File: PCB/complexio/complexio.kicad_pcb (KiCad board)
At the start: 2 copper layers, 69.1 x 144.1 mm, 107 parts, among them J1 Conn_01x21_Pin, J2 Conn_01x21_Pin, J3 USB_C_Receptacle_USB2.0_16P, J5 Conn_01x03_Pin, Q1 AO3400A, SW1 SW_SPDT, U1 MPU6050, U10 KTIR0711S, U11 KTIR0711S, U12 KTIR0711S, U13 KTIR0711S, U14 KTIR0711S, U15 KTIR0711S, U16 KTIR0711S, U17 KTIR0711S, U18 KTIR0711S, U19 KTIR0711S, U2 TB6612FNG, U20 SN74LVC16T245DGGR, U21 AT24CM01, U22 STM32F303RBT6, U23 AP2112K-3.3, U3 TB6612FNG, U4 KTIR0711S, U5 KTIR0711S, U6 KTIR0711S, U7 KTIR0711S, U8 KTIR0711S, U9 KTIR0711S

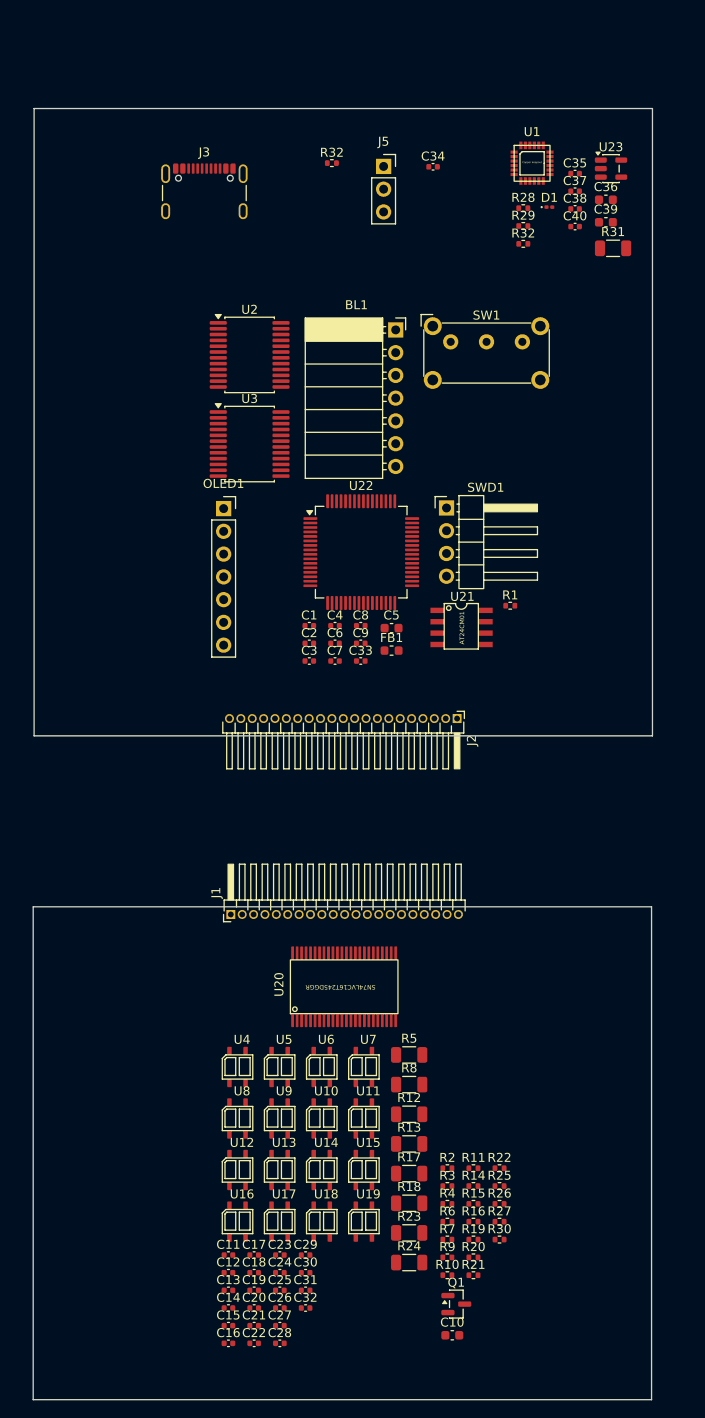
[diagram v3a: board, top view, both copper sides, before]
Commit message: Advanced with schem & resolved main power problem
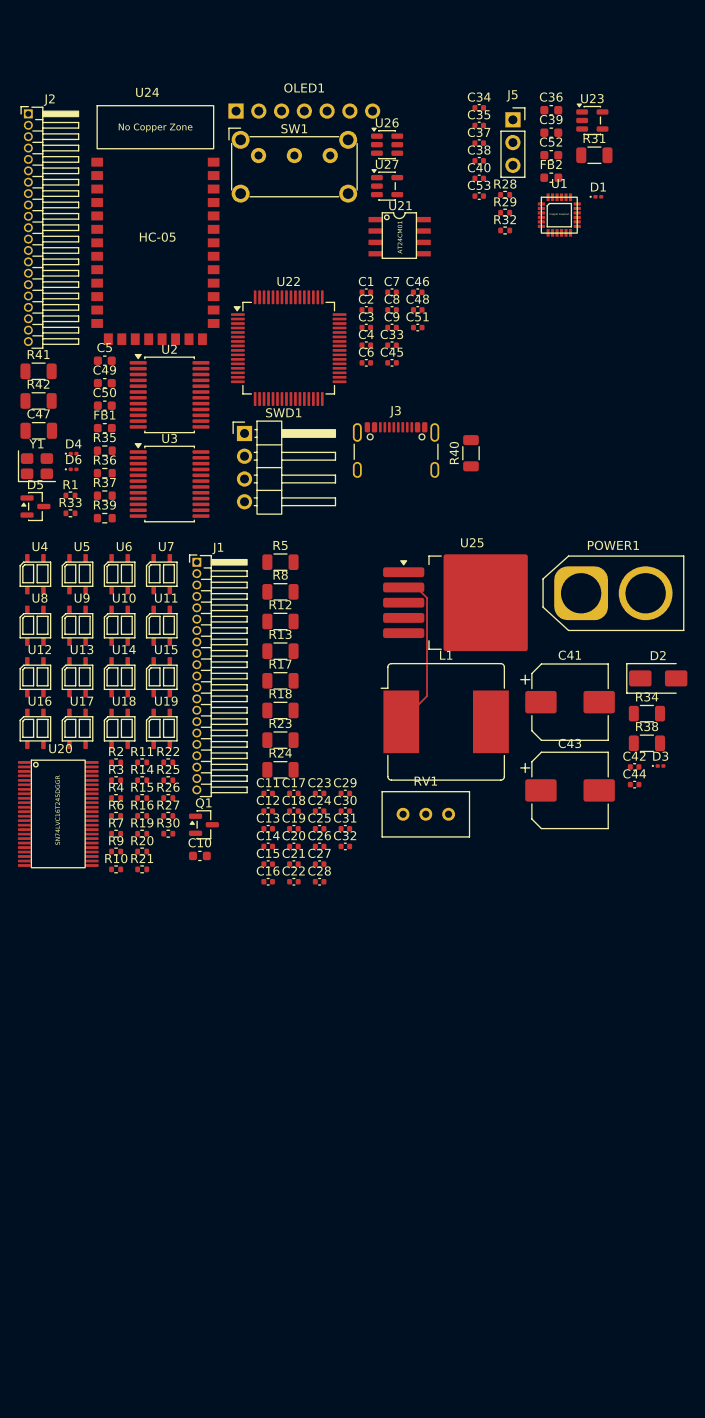
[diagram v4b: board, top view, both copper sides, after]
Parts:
- removed BL1: Bluetooth HC-05 module, Connector_PinSocket_2.54mm:PinSocket_1x07_P2.54mm_Horizontal
- removed the R32 at (116.2, 59.1)
- removed the R32 at (137.6, 68.1)
- added C41: 100u, Capacitor_SMD:CP_Elec_8x10, F.Cu at (142.8, 119.2)
- added C42: 100n, Capacitor_SMD:C_0402_1005Metric, F.Cu at (150.0, 126.5)
- added C43: 220u, Capacitor_SMD:CP_Elec_8x10, F.Cu at (142.8, 129.1)
- added C44: 100n, Capacitor_SMD:C_0402_1005Metric, F.Cu at (150.0, 128.4)
- added C45: 18p, Capacitor_SMD:C_0402_1005Metric, F.Cu at (122.9, 81.4)
- added C46: 18p, Capacitor_SMD:C_0402_1005Metric, F.Cu at (125.8, 73.5)
- added C47: 4n7, Capacitor_SMD:C_1206_3216Metric, F.Cu at (83.5, 89.0)
- added C48: 100n, Capacitor_SMD:C_0402_1005Metric, F.Cu at (125.8, 75.5)
- added C49: 4u7, Capacitor_SMD:C_0603_1608Metric, F.Cu at (90.9, 83.7)
- added C50: 10u, Capacitor_SMD:C_0603_1608Metric, F.Cu at (90.9, 86.2)
- added C51: 100n, Capacitor_SMD:C_0402_1005Metric, F.Cu at (125.8, 77.4)
- added C52: 10u, Capacitor_SMD:C_0603_1608Metric, F.Cu at (140.7, 58.2)
- added C53: 100n, Capacitor_SMD:C_0402_1005Metric, F.Cu at (132.7, 62.8)
- added D2: SS34, Diode_SMD:D_SMA, F.Cu at (152.6, 116.6)
- added D3: LED, LED_SMD:LED_0201_0603Metric, F.Cu at (152.9, 126.4)
- added D4: LED, LED_SMD:LED_0201_0603Metric, F.Cu at (87.4, 91.5)
- added D5: BAT54C, Package_TO_SOT_SMD:SOT-23, F.Cu at (83.2, 97.4)
- added D6: LED, LED_SMD:LED_0201_0603Metric, F.Cu at (87.4, 93.3)
- added FB2: 600R, Inductor_SMD:L_0603_1608Metric, F.Cu at (140.7, 60.7)
- added L1: 47uH, Inductor_SMD:L_Bourns_SRR1208_12.7x12.7mm, F.Cu at (129.0, 121.4)
- added POWER1: Conn_01x02_Socket, Connector_AMASS:AMASS_XT60-M_1x02_P7.20mm_Vertical, F.Cu at (144.0, 107.1)
- added R32: 4k7, Resistor_SMD:R_0402_1005Metric, F.Cu at (135.6, 66.6)
- added R33: 10k, Resistor_SMD:R_0402_1005Metric, F.Cu at (87.1, 98.2)
- added R34: 1k, Resistor_SMD:R_1206_3216Metric, F.Cu at (151.4, 120.5)
- added R35: 2k2, Resistor_SMD:R_0603_1608Metric, F.Cu at (90.9, 91.2)
- added R36: 2k2, Resistor_SMD:R_0603_1608Metric, F.Cu at (90.9, 93.7)
- added R37: 5k1, Resistor_SMD:R_0603_1608Metric, F.Cu at (90.9, 96.2)
- added R38: 1k, Resistor_SMD:R_1206_3216Metric, F.Cu at (151.4, 123.8)
- added R39: 5k1, Resistor_SMD:R_0603_1608Metric, F.Cu at (90.9, 98.7)
- added R40: 1M, Resistor_SMD:R_1206_3216Metric, F.Cu at (131.8, 91.5)
- added R41: 1k, Resistor_SMD:R_1206_3216Metric, F.Cu at (83.5, 82.3)
- added R42: 1k, Resistor_SMD:R_1206_3216Metric, F.Cu at (83.5, 85.6)
- added RV1: R_Potentiometer, Potentiometer_THT:Potentiometer_Bourns_3296W_Vertical, F.Cu at (129.2, 131.8)
- added U24: HC-05, HC-05:HC-05_SMD, F.Cu at (90.0, 52.7)
- added U25: LM2596S-ADJ, Package_TO_SOT_SMD:TO-263-5_TabPin3, F.Cu at (131.9, 108.1)
- added U26: USBLC6-2SC6, Package_TO_SOT_SMD:SOT-23-6, F.Cu at (122.4, 57.0)
- added U27: AP2112K-3.3, Package_TO_SOT_SMD:SOT-23-5, F.Cu at (122.4, 61.7)
- added Y1: 8MHz, Crystal:Crystal_SMD_3225-4Pin_3.2x2.5mm, F.Cu at (83.3, 92.9)
- OLED1: footprint Connector_PinSocket_2.54mm:PinSocket_1x07_P2.54mm_Vertical -> SSD1306_SPI:SSD1306_SPI
- moved J2 82.7 mm to (82.4, 53.6), turned to 0 degrees
- moved Q1 60.4 mm to (102.0, 132.9)
- moved C10 60.4 mm to (101.5, 136.4)
- moved U10 59.4 mm to (90.8, 108.5)
- moved U11 59.4 mm to (95.5, 108.5)
- moved U12 59.4 mm to (81.4, 114.2)
- moved U13 59.4 mm to (86.1, 114.2)
- moved U14 59.4 mm to (90.8, 114.2)
- moved U15 59.4 mm to (95.5, 114.2)
- moved U16 59.4 mm to (81.4, 120.0)
- moved U17 59.4 mm to (86.1, 120.0)
- moved U18 59.4 mm to (90.8, 120.0)
- moved U19 59.4 mm to (95.5, 120.0)
- moved U4 59.4 mm to (81.4, 102.7)
- moved U5 59.4 mm to (86.1, 102.7)
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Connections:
- net /PA14 renamed /SWCLK
- net Net-(J3-VBUS-PadA4) renamed VBUS_5V
- C10 pad 1: +5V -> BAT_5V
- C11 pad 1: +5V -> BAT_5V
- C12 pad 1: +5V -> BAT_5V
- C13 pad 1: +5V -> BAT_5V
- C14 pad 1: +5V -> BAT_5V
- C15 pad 1: +5V -> BAT_5V
- C16 pad 1: +5V -> BAT_5V
- C17 pad 1: +5V -> BAT_5V
- C18 pad 1: +5V -> BAT_5V
- C19 pad 1: +5V -> BAT_5V
- C20 pad 1: +5V -> BAT_5V
- C21 pad 1: +5V -> BAT_5V
- C22 pad 1: +5V -> BAT_5V
- C23 pad 1: +5V -> BAT_5V
- C24 pad 1: +5V -> BAT_5V
- C25 pad 1: +5V -> BAT_5V
- C26 pad 1: +5V -> BAT_5V
- C27 pad 1: +5V -> BAT_5V
- C28 pad 1: +5V -> BAT_5V
- C36 pad 1: +5V -> MAIN_5V
- C37 pad 1: VDD -> IMU_VDD
- C38 pad 1: VDD -> IMU_VDD
- C39 pad 1: VDD -> +3V3
- C40 pad 1: VDD -> +3V3
- J1 pad 1: +5V -> BAT_5V
- J1 pad 10: /Sensor_array/sen5 -> /sen5
- J1 pad 11: /Sensor_array/sen6 -> /sen6
- J1 pad 12: /Sensor_array/sen7 -> /sen7
- J1 pad 13: /Sensor_array/sen8 -> /sen8
- J1 pad 14: /Sensor_array/sen9 -> /sen9
- J1 pad 15: /Sensor_array/sen10 -> /sen10
- J1 pad 16: /Sensor_array/sen11 -> /sen11
- J1 pad 17: /Sensor_array/sen12 -> /sen12
- J1 pad 18: /Sensor_array/sen13 -> /sen13
- J1 pad 19: /Sensor_array/sen14 -> /sen14
- J1 pad 20: /Sensor_array/sen15 -> /sen15
- J1 pad 21: /Sensor_array/sen16 -> /sen16
- J1 pad 4: /Sensor_array/oe -> /oe
- J1 pad 5: /Sensor_array/ledon -> /ledon
- J1 pad 6: /Sensor_array/sen1 -> /sen1
- J1 pad 7: /Sensor_array/sen2 -> /sen2
- J1 pad 8: /Sensor_array/sen3 -> /sen3
- J1 pad 9: /Sensor_array/sen4 -> /sen4
- J2 pad 1: /Sensor_array/sen16 -> /sen16
- J2 pad 10: /Sensor_array/sen7 -> /sen7
- J2 pad 11: /Sensor_array/sen6 -> /sen6
- J2 pad 12: /Sensor_array/sen5 -> /sen5
- J2 pad 13: /Sensor_array/sen4 -> /sen4
- J2 pad 14: /Sensor_array/sen3 -> /sen3
- J2 pad 15: /Sensor_array/sen2 -> /sen2
- J2 pad 16: /Sensor_array/sen1 -> /sen1
- J2 pad 17: /Sensor_array/ledon -> /ledon
- J2 pad 18: /Sensor_array/oe -> /oe
- J2 pad 2: /Sensor_array/sen15 -> /sen15
- J2 pad 21: +5V -> BAT_5V
- J2 pad 3: /Sensor_array/sen14 -> /sen14
- J2 pad 4: /Sensor_array/sen13 -> /sen13
- J2 pad 5: /Sensor_array/sen12 -> /sen12
- J2 pad 6: /Sensor_array/sen11 -> /sen11
- J2 pad 7: /Sensor_array/sen10 -> /sen10
- J2 pad 8: /Sensor_array/sen9 -> /sen9
- J2 pad 9: /Sensor_array/sen8 -> /sen8
- J3 pad A1: Net-(J3-GND-PadA1) -> GND
- J3 pad A12: Net-(J3-GND-PadA1) -> GND
- J3 pad A5: unconnected-(J3-CC1-PadA5) -> Net-(J3-CC1)
- J3 pad A6: unconnected-(J3-D+-PadA6) -> Net-(J3-D+-PadA6)
- J3 pad A7: unconnected-(J3-D--PadA7) -> Net-(J3-D--PadA7)
- J3 pad B1: Net-(J3-GND-PadA1) -> GND
- J3 pad B12: Net-(J3-GND-PadA1) -> GND
- J3 pad B5: unconnected-(J3-CC2-PadB5) -> Net-(J3-CC2)
- J3 pad B6: unconnected-(J3-D+-PadB6) -> Net-(J3-D+-PadA6)
- J3 pad B7: unconnected-(J3-D--PadB7) -> Net-(J3-D--PadA7)
- J3 pad S1: unconnected-(J3-SHIELD-PadS1) -> Net-(J3-SHIELD)
- J5 pad 1: VDD -> +3V3
- OLED1 pad 1: unconnected-(OLED1-GND-Pad1) -> GND
- OLED1 pad 2: unconnected-(OLED1-VCC-Pad2) -> +5V
- OLED1 pad 3: unconnected-(OLED1-CLK-Pad3) -> /SPI_CLK
- OLED1 pad 4: unconnected-(OLED1-MOSI-Pad4) -> /SPI_MOSI
- OLED1 pad 5: unconnected-(OLED1-RES-Pad5) -> /SPI_RES
- OLED1 pad 6: unconnected-(OLED1-DC-Pad6) -> /SPI_DC
- OLED1 pad 7: unconnected-(OLED1-CS-Pad7) -> /SPI_CS
- Q1 pad 1: /Sensor_array/ledon -> /ledon
- R10 pad 2: +5V -> BAT_5V
- R11 pad 1: /Sensor_array/ledon -> /ledon
- R11 pad 2: +5V -> BAT_5V
- R12 pad 1: +5V -> BAT_5V
- R13 pad 1: +5V -> BAT_5V
- R14 pad 2: +5V -> BAT_5V
- R15 pad 2: +5V -> BAT_5V
- R16 pad 2: +5V -> BAT_5V
- R17 pad 1: +5V -> BAT_5V
- R18 pad 1: +5V -> BAT_5V
- R19 pad 2: +5V -> BAT_5V
- R2 pad 2: +5V -> BAT_5V
- R20 pad 2: +5V -> BAT_5V
- R21 pad 2: +5V -> BAT_5V
- R22 pad 2: +5V -> BAT_5V
- R23 pad 1: +5V -> BAT_5V
- R24 pad 1: +5V -> BAT_5V
- R25 pad 2: +5V -> BAT_5V
- R26 pad 2: +5V -> BAT_5V
- R27 pad 2: /Sensor_array/oe -> /oe
- R28 pad 1: /PB8 -> /I2C_SCL
- R28 pad 2: VDD -> IMU_VDD
- R29 pad 1: /PB9 -> /I2C_SDA
- R29 pad 2: VDD -> IMU_VDD
- R3 pad 2: +5V -> BAT_5V
- R30 pad 2: /Sensor_array/oe -> /oe
- R31 pad 2: VDD -> +3V3
- R4 pad 2: +5V -> BAT_5V
- R5 pad 1: +5V -> BAT_5V
- R6 pad 2: +5V -> BAT_5V
- R7 pad 2: +5V -> BAT_5V
- R8 pad 1: +5V -> BAT_5V
- R9 pad 2: +5V -> BAT_5V
- SWD1 pad 1: /PA13 -> GND
- SWD1 pad 2: GND -> /SWDIO
- U1 pad 13: VDD -> IMU_VDD
- U1 pad 23: /PB8 -> /I2C_SCL
- U1 pad 24: /PB9 -> /I2C_SDA
- U1 pad 8: VDD -> IMU_VDD
- U20 pad 18: +5V -> BAT_5V
- U20 pad 25: /Sensor_array/oe -> /oe
- U20 pad 26: /Sensor_array/sen16 -> /sen16
- U20 pad 27: /Sensor_array/sen15 -> /sen15
- U20 pad 29: /Sensor_array/sen14 -> /sen14
- U20 pad 30: /Sensor_array/sen13 -> /sen13
- U20 pad 32: /Sensor_array/sen12 -> /sen12
- U20 pad 33: /Sensor_array/sen11 -> /sen11
- U20 pad 35: /Sensor_array/sen10 -> /sen10
- U20 pad 36: /Sensor_array/sen9 -> /sen9
- U20 pad 37: /Sensor_array/sen8 -> /sen8
- U20 pad 38: /Sensor_array/sen7 -> /sen7
- U20 pad 40: /Sensor_array/sen6 -> /sen6
- U20 pad 41: /Sensor_array/sen5 -> /sen5
- U20 pad 43: /Sensor_array/sen4 -> /sen4
- U20 pad 44: /Sensor_array/sen3 -> /sen3
- U20 pad 46: /Sensor_array/sen2 -> /sen2
- U20 pad 47: /Sensor_array/sen1 -> /sen1
- U20 pad 48: /Sensor_array/oe -> /oe
- U20 pad 7: +5V -> BAT_5V
- U21 pad 2: unconnected-(U21-A1-Pad2) -> GND
- U21 pad 3: unconnected-(U21-A2-Pad3) -> GND
- U21 pad 4: unconnected-(U21-GND-Pad4) -> GND
- U21 pad 5: unconnected-(U21-SDA-Pad5) -> /I2C_SDA
- U21 pad 6: unconnected-(U21-SCL-Pad6) -> /I2C_SCL
- U21 pad 7: unconnected-(U21-WP-Pad7) -> /WP
- U21 pad 8: unconnected-(U21-VCC-Pad8) -> +3V3
- U22 pad 10: unconnected-(U22-PC2-Pad10) -> /sen3
- U22 pad 14: unconnected-(U22-PA0-Pad14) -> /sen4
- U22 pad 15: unconnected-(U22-PA1-Pad15) -> /sen5
- U22 pad 16: unconnected-(U22-PA2-Pad16) -> /sen6
- U22 pad 17: unconnected-(U22-PA3-Pad17) -> /sen7
- U22 pad 18: unconnected-(U22-PF4-Pad18) -> /sen8
- U22 pad 2: unconnected-(U22-PC13-Pad2) -> /LED
- U22 pad 20: unconnected-(U22-PA4-Pad20) -> /sen9
- U22 pad 21: unconnected-(U22-PA5-Pad21) -> /sen10
- U22 pad 22: unconnected-(U22-PA6-Pad22) -> /sen11
- U22 pad 23: unconnected-(U22-PA7-Pad23) -> /sen12
- U22 pad 24: unconnected-(U22-PC4-Pad24) -> /sen13
- U22 pad 27: unconnected-(U22-PB1-Pad27) -> /sen14
- U22 pad 29: unconnected-(U22-PB10-Pad29) -> /oe
- U22 pad 33: unconnected-(U22-PB12-Pad33) -> /sen15
- U22 pad 35: unconnected-(U22-PB14-Pad35) -> /sen16
- U22 pad 37: unconnected-(U22-PC6-Pad37) -> /bin2
- U22 pad 38: unconnected-(U22-PC7-Pad38) -> /bin1
- U22 pad 39: unconnected-(U22-PC8-Pad39) -> /ain2
- U22 pad 40: unconnected-(U22-PC9-Pad40) -> /ain1
- U22 pad 41: unconnected-(U22-PA8-Pad41) -> /pwma
- U22 pad 42: unconnected-(U22-PA9-Pad42) -> /pwmb
- U22 pad 43: unconnected-(U22-PA10-Pad43) -> /ledon
- U22 pad 44: unconnected-(U22-PA11-Pad44) -> /USB_C_D-
- U22 pad 45: unconnected-(U22-PA12-Pad45) -> /USB_C_D+
- U22 pad 46: /PA13 -> /SWDIO
- U22 pad 5: unconnected-(U22-PF0-Pad5) -> /HSE_IN
- U22 pad 50: /PA15 -> unconnected-(U22-PA15-Pad50)
- U22 pad 52: unconnected-(U22-PC11-Pad52) -> /UART_RX
- U22 pad 53: unconnected-(U22-PC12-Pad53) -> /UART_TX
- U22 pad 54: unconnected-(U22-PD2-Pad54) -> /SPI_RES
- U22 pad 55: unconnected-(U22-PB3-Pad55) -> /SPI_CLK
- U22 pad 56: unconnected-(U22-PB4-Pad56) -> /SPI_DC
- U22 pad 57: unconnected-(U22-PB5-Pad57) -> /SPI_MOSI
- U22 pad 58: unconnected-(U22-PB6-Pad58) -> /SPI_CS
- U22 pad 59: unconnected-(U22-PB7-Pad59) -> /WP
- U22 pad 6: unconnected-(U22-PF1-Pad6) -> /HSE_OUT
- U22 pad 61: unconnected-(U22-PB8-Pad61) -> /I2C_SCL
- U22 pad 62: unconnected-(U22-PB9-Pad62) -> /I2C_SDA
- U22 pad 8: unconnected-(U22-PC0-Pad8) -> /sen1
- U22 pad 9: unconnected-(U22-PC1-Pad9) -> /sen2
- U23 pad 1: +5V -> MAIN_5V
- U23 pad 3: +5V -> MAIN_5V
- U23 pad 5: VDD -> +3V3
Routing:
- net Net-(D2-K): track 0.00 -> 18.1 mm
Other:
- board outline removed
